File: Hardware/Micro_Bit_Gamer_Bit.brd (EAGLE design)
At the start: 152.4 x 50.8 mm, 35 parts, among them J1 Pokehome, J2 Pokehome, J3 Pokehome, J4 Pokehome, J5 Pokehome, J6 Pokehome, J7 Pokehome, J8 Pokehome, U1 micro:bit

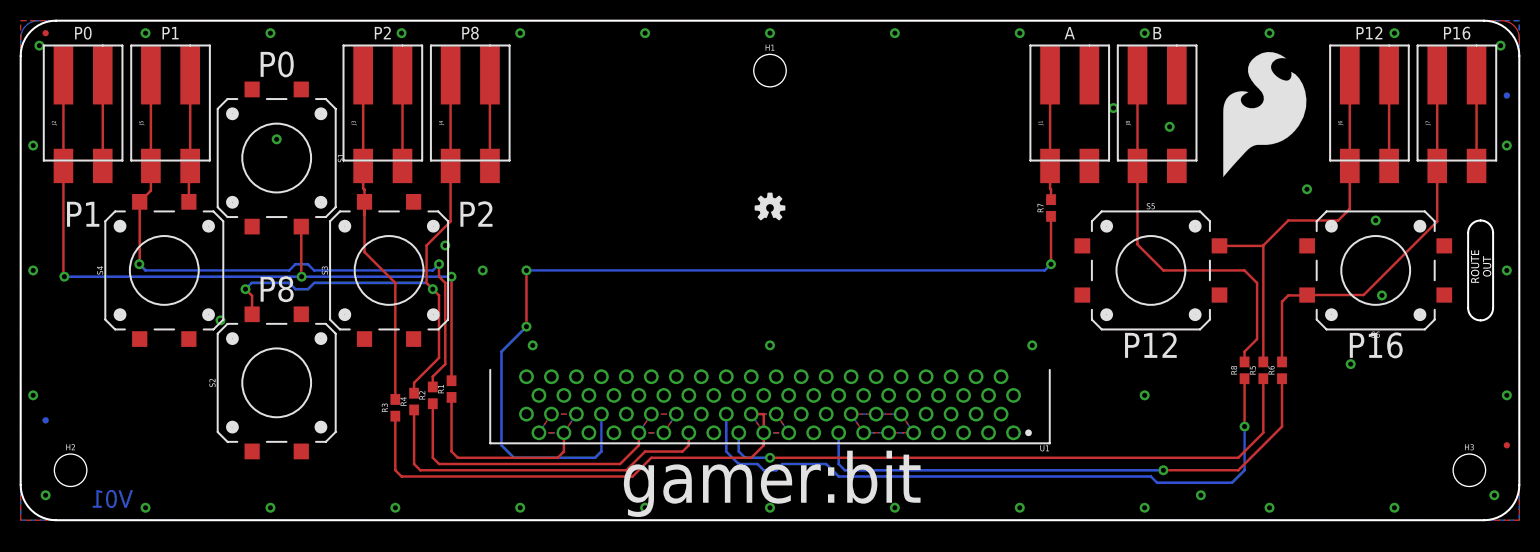
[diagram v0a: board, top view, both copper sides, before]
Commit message: Incorporating Edu Feedback.
Pokehomes on back of board.
Touched up logos & markings.
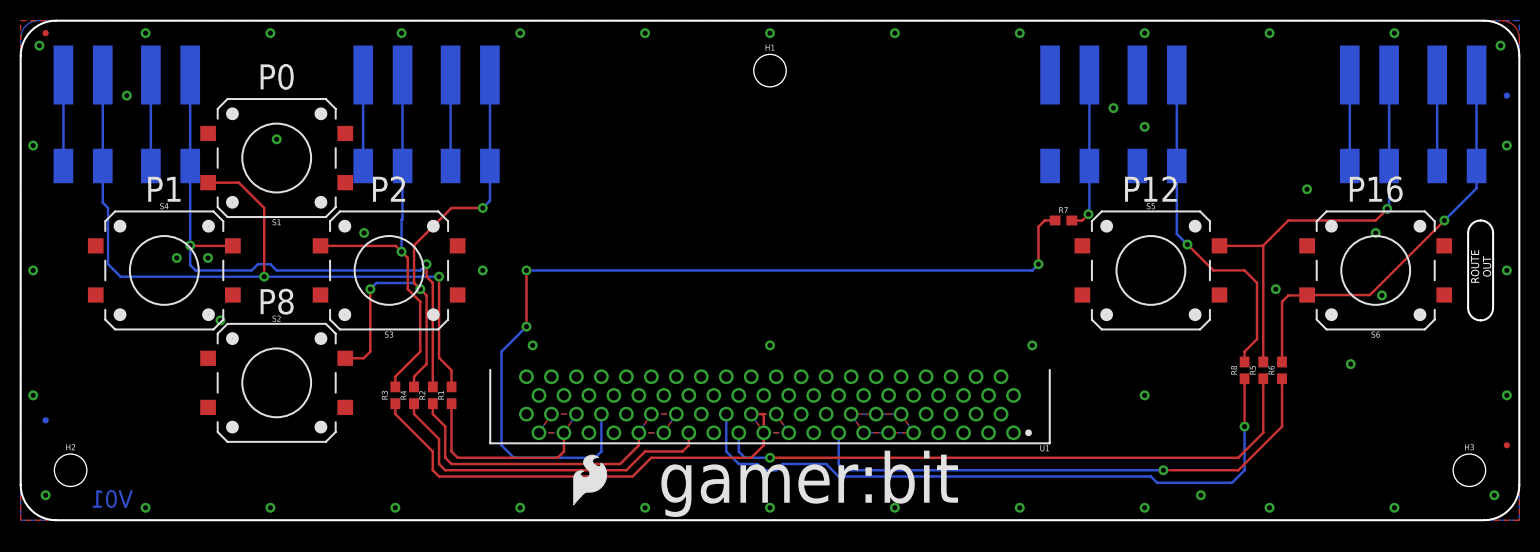
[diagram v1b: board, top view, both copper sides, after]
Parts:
- LOGO1: value SFE_LOGO_FLAME.5_INCH -> SFE_LOGO_FLAME.2_INCH; device SparkFun-Aesthetics:SFE_LOGO_FLAME_.5 -> SparkFun-Aesthetics:SFE_LOGO_FLAME_.2
- moved LOGO1 74.0 mm to (55.9, 1.27)
- moved LOGO3 14.0 mm to (92.7, 34.3)
- moved LOGO2 6.35 mm to (76.2, 25.4), flipped to the bottom
- moved R7 1.80 mm to (106.0, 30.5), turned to 0 degrees
- moved R3 1.27 mm to (38.1, 12.7)
- moved R1 0.64 mm to (43.8, 12.7)
- moved R4 0.63 mm to (40.0, 12.7)
- flipped J1 to the bottom
- flipped J2 to the bottom
- flipped J3 to the bottom
- flipped J4 to the bottom
- flipped J5 to the bottom
- flipped J6 to the bottom
- flipped J7 to the bottom
- flipped J8 to the bottom
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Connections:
- net GND: now also S3.3; no longer S3.1
- net N$4: now also S3.1; no longer S3.3
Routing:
- net N$4: track 35.6 -> 42.2 mm, vias 0 -> 1
- net N$3: track 57.9 -> 52.6 mm, vias 2 -> 3
- net N$6: track 39.6 -> 35.0 mm, vias 0 -> 1
- net N$80: track 40.3 -> 44.2 mm, vias 0 -> 1
- net N$1: track 75.6 -> 79.2 mm, vias 3 -> 2
- net N$7: track 12.7 -> 16.2 mm, vias 0 -> 1
- net N$2: track 64.5 -> 61.5 mm
- net GND: track 58.4 -> 55.5 mm, vias 47 -> 51
- net N$5: track 40.2 -> 42.2 mm, vias 0 -> 1
- net BTN_R: track 49.0 -> 48.0 mm
- net BTN_DN: track 36.0 -> 35.2 mm
- net BTN_L: track 28.8 -> 28.0 mm
- net BTN_UP: track 19.4 -> 18.7 mm
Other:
- board text added: "sparkfun.com/microbit"

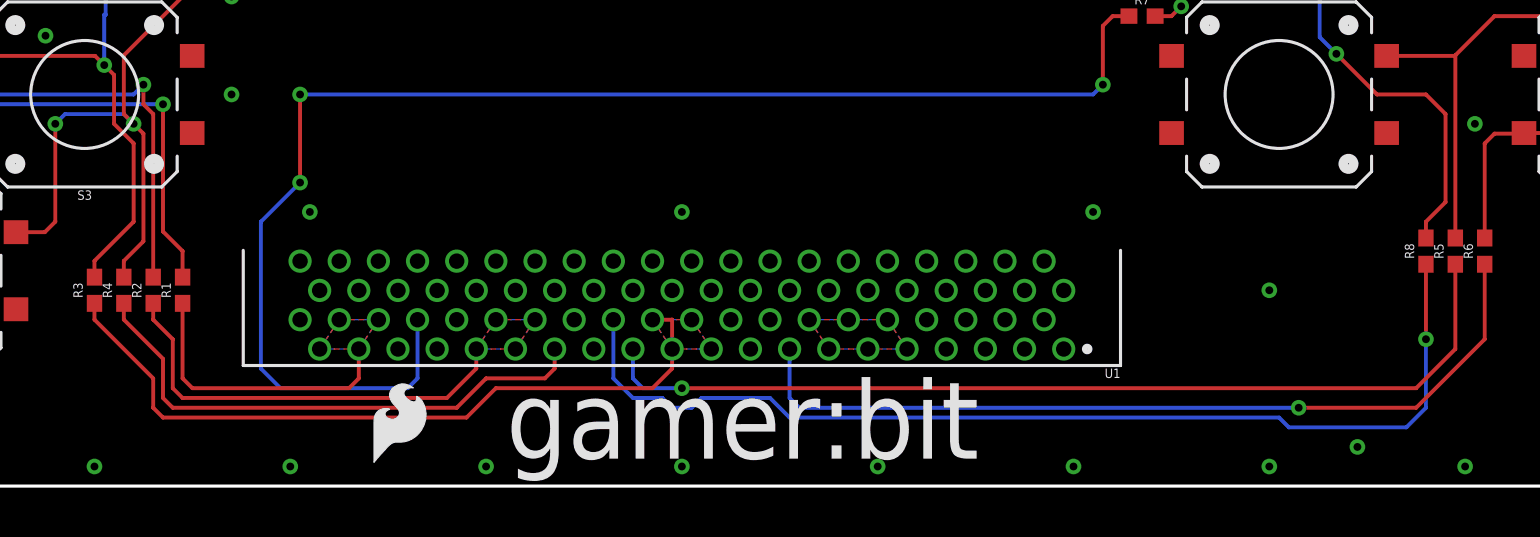
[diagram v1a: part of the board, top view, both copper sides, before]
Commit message: Changed name font to match other microbit boards
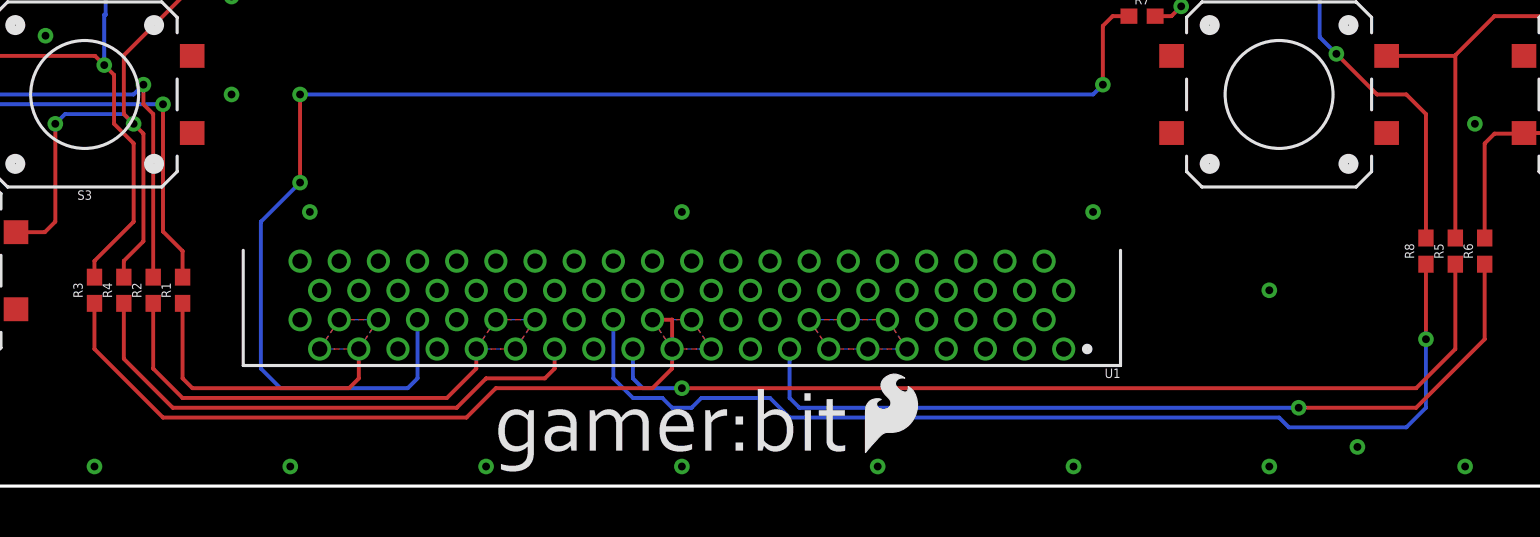
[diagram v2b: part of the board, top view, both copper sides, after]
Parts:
- added U$2, U$3: LOGO-GAMERBIT, Micro_Bit_Parts:LOGO-GAMERBIT
- moved LOGO1 31.9 mm to (87.8, 1.91)
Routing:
- net N$6: track 35.0 -> 33.2 mm
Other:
- board text removed: "gamer:bit"
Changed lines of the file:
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@@
 <setting verticaltext="up"/>
 </settings>
-<grid distance="0.025" unitdist="inch" unit="inch" style="lines" multiple="1" display="yes" altdistance="0.005" altunitdist="inch" altunit="inch"/>
+<grid distance="0.05" unitdist="inch" unit="inch" style="lines" multiple="1" display="yes" altdistance="0.005" altunitdist="inch" altunit="inch"/>
 <layers>
 <layer number="1" name="Top" color="4" fill="1" visible="yes" active="yes"/>
@@
 <layer number="22" name="bPlace" color="14" fill="1" visible="yes" active="yes"/>
 <layer number="23" name="tOrigins" color="15" fill="1" visible="yes" active="yes"/>
-<layer number="24" name="bOrigins" color="15" fill="1" visible="no" active="yes"/>
-<layer number="25" name="tNames" color="7" fill="1" visible="yes" active="yes"/>
+<layer number="24" name="bOrigins" color="15" fill="1" visible="yes" active="yes"/>
+<layer number="25" name="tNames" color="7" fill="1" visible="no" active="yes"/>
 <layer number="26" name="bNames" color="7" fill="1" visible="no" active="yes"/>
 <layer number="27" name="tValues" color="7" fill="1" visible="no" active="yes"/>
@@
 <layer number="49" name="Reference" color="7" fill="1" visible="no" active="yes"/>
 <layer number="50" name="dxf" color="7" fill="1" visible="no" active="no"/>
-<layer number="51" name="tDocu" color="6" fill="1" visible="yes" active="yes"/>
+<layer number="51" name="tDocu" color="6" fill="1" visible="no" active="yes"/>
 <layer number="52" name="bDocu" color="7" fill="1" visible="no" active="yes"/>
 <layer number="53" name="tGND_GNDA" color="7" fill="9" visible="no" active="no"/>
@@
 <text x="114.935" y="32.385" size="2.54" layer="21" font="vector" ratio="15" align="bottom-center">P12</text>
 <text x="137.795" y="32.385" size="2.54" layer="21" font="vector" ratio="15" align="bottom-center">P16</text>
-<text x="80.137" y="1.778" size="5.08" layer="21" font="vector" ratio="15" align="bottom-center">gamer:bit</text>
 <text x="6.35" y="48.895" size="1.27" layer="22" font="vector" ratio="15" rot="MR0" align="bottom-center">P0</text>
 <text x="15.24" y="48.895" size="1.27" layer="22" font="vector" ratio="15" rot="MR0" align="bottom-center">P1</text>
@@
 <text x="137.16" y="48.895" size="1.27" layer="22" font="vector" ratio="15" rot="MR0" align="bottom-center">P12</text>
 <text x="146.05" y="48.895" size="1.27" layer="22" font="vector" ratio="15" rot="MR0" align="bottom-center">P16</text>
-<text x="76.073" y="28.448" size="3.81" layer="22" font="vector" ratio="15" rot="MR0" align="bottom-center">gamer:bit</text>
 <text x="11.43" y="1.27" size="1.778" layer="16" font="vector" ratio="15" rot="MR0">V01</text>
 <dimension x1="0" y1="50.8" x2="152.4" y2="50.8" x3="76.2" y3="88.265" textsize="1.778" textratio="15" layer="47" unit="inch"/>
@@
 <attribute name="PROD_ID" value="CONN-13512" x="146.05" y="41.275" size="1.778" layer="28" font="vector" ratio="15" rot="MR270" display="off"/>
 </element>
-<element name="LOGO1" library="SparkFun-Aesthetics" package="SFE_LOGO_FLAME_.2" value="SFE_LOGO_FLAME.2_INCH" x="55.88" y="1.27"/>
+<element name="LOGO1" library="SparkFun-Aesthetics" package="SFE_LOGO_FLAME_.2" value="SFE_LOGO_FLAME.2_INCH" x="87.757" y="1.905"/>
 <element name="LOGO2" library="SparkFun-Aesthetics" package="OSHW-LOGO-S" value="OSHW-LOGOS" x="76.2" y="25.4" rot="MR0"/>
 <element name="LOGO3" library="SparkFun-Aesthetics" package="SFE_LOGO_NAME_FLAME_.3" value="SFE_LOGO_NAME_FLAME.3_INCH" x="92.71" y="34.29" rot="MR0"/>
@@
 <element name="FD3" library="SparkFun-Aesthetics" package="FIDUCIAL-MICRO" value="FIDUCIALUFIDUCIAL" x="2.54" y="10.16" rot="MR0"/>
 <element name="FD4" library="SparkFun-Aesthetics" package="FIDUCIAL-MICRO" value="FIDUCIALUFIDUCIAL" x="151.13" y="43.18" rot="MR0"/>
+<element name="U$2" library="Micro_Bit_Parts" package="LOGO-GAMERBIT" value="LOGO-GAMERBIT" x="64.135" y="0.762"/>
+<element name="U$3" library="Micro_Bit_Parts" package="LOGO-GAMERBIT" value="LOGO-GAMERBIT" x="87.63" y="27.813" rot="MR0"/>
 </elements>
 <signals>
@@
 <wire x1="60.96" y1="5.715" x2="43.815" y2="5.715" width="0.254" layer="1"/>
 <contactref element="R2" pad="1"/>
-<wire x1="41.91" y1="11.85" x2="41.91" y2="10.795" width="0.254" layer="1"/>
-<wire x1="41.91" y1="10.795" x2="43.18" y2="9.525" width="0.254" layer="1"/>
-<wire x1="43.18" y1="9.525" x2="43.18" y2="6.35" width="0.254" layer="1"/>
-<wire x1="43.18" y1="6.35" x2="43.815" y2="5.715" width="0.254" layer="1"/>
+<wire x1="41.91" y1="11.85" x2="41.91" y2="7.62" width="0.254" layer="1"/>
+<wire x1="41.91" y1="7.62" x2="43.815" y2="5.715" width="0.254" layer="1"/>
 </signal>
 <signal name="BTN_R">
@@
 <wire x1="62.23" y1="4.445" x2="42.545" y2="4.445" width="0.254" layer="1"/>
 <contactref element="R3" pad="1"/>
-<wire x1="42.545" y1="4.445" x2="41.91" y2="5.08" width="0.254" layer="1"/>
-<wire x1="38.1" y1="11.85" x2="38.1" y2="10.795" width="0.254" layer="1"/>
-<wire x1="38.1" y1="10.795" x2="41.91" y2="6.985" width="0.254" layer="1"/>
-<wire x1="41.91" y1="6.985" x2="41.91" y2="5.08" width="0.254" layer="1"/>
+<wire x1="38.1" y1="11.85" x2="38.1" y2="8.89" width="0.254" layer="1"/>
+<wire x1="38.1" y1="8.89" x2="42.545" y2="4.445" width="0.254" layer="1"/>
 </signal>
 <signal name="BTN_DN">
@@
 <wire x1="61.595" y1="5.08" x2="43.18" y2="5.08" width="0.254" layer="1"/>
 <contactref element="R4" pad="1"/>
-<wire x1="40.005" y1="11.85" x2="40.005" y2="10.795" width="0.254" layer="1"/>
-<wire x1="40.005" y1="10.795" x2="42.545" y2="8.255" width="0.254" layer="1"/>
-<wire x1="42.545" y1="8.255" x2="42.545" y2="5.715" width="0.254" layer="1"/>
-<wire x1="42.545" y1="5.715" x2="43.18" y2="5.08" width="0.254" layer="1"/>
+<wire x1="40.005" y1="11.85" x2="40.005" y2="8.255" width="0.254" layer="1"/>
+<wire x1="40.005" y1="8.255" x2="43.18" y2="5.08" width="0.254" layer="1"/>
 </signal>
 <signal name="BTN_P16">
@@
 <contactref element="J8" pad="P4"/>
 <contactref element="J8" pad="P2"/>
-<wire x1="124.46" y1="16.09" x2="124.46" y2="17.145" width="0.254" layer="1"/>
-<wire x1="124.46" y1="17.145" x2="125.73" y2="18.415" width="0.254" layer="1"/>
-<wire x1="125.73" y1="18.415" x2="125.73" y2="24.13" width="0.254" layer="1"/>
-<wire x1="125.73" y1="24.13" x2="124.46" y2="25.4" width="0.254" layer="1"/>
-<wire x1="124.46" y1="25.4" x2="121.285" y2="25.4" width="0.254" layer="1"/>
+<wire x1="124.46" y1="16.09" x2="124.46" y2="24.13" width="0.254" layer="1"/>
+<wire x1="124.46" y1="24.13" x2="123.19" y2="25.4" width="0.254" layer="1"/>
+<wire x1="123.19" y1="25.4" x2="121.285" y2="25.4" width="0.254" layer="1"/>
 <wire x1="118.65" y1="28.035" x2="121.285" y2="25.4" width="0.254" layer="1"/>
 <wire x1="117.57" y1="36.025" x2="117.57" y2="45.275" width="0.254" layer="16"/>

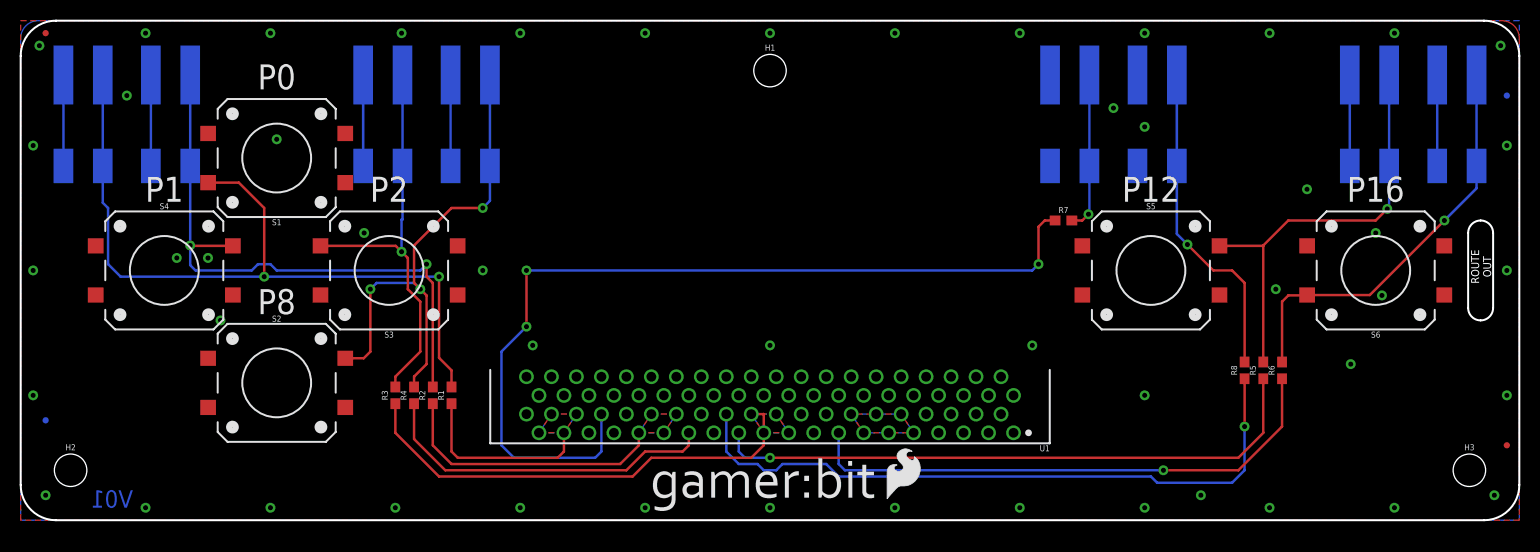
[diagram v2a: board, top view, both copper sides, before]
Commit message: Moved right two buttons together by 0.3 inches
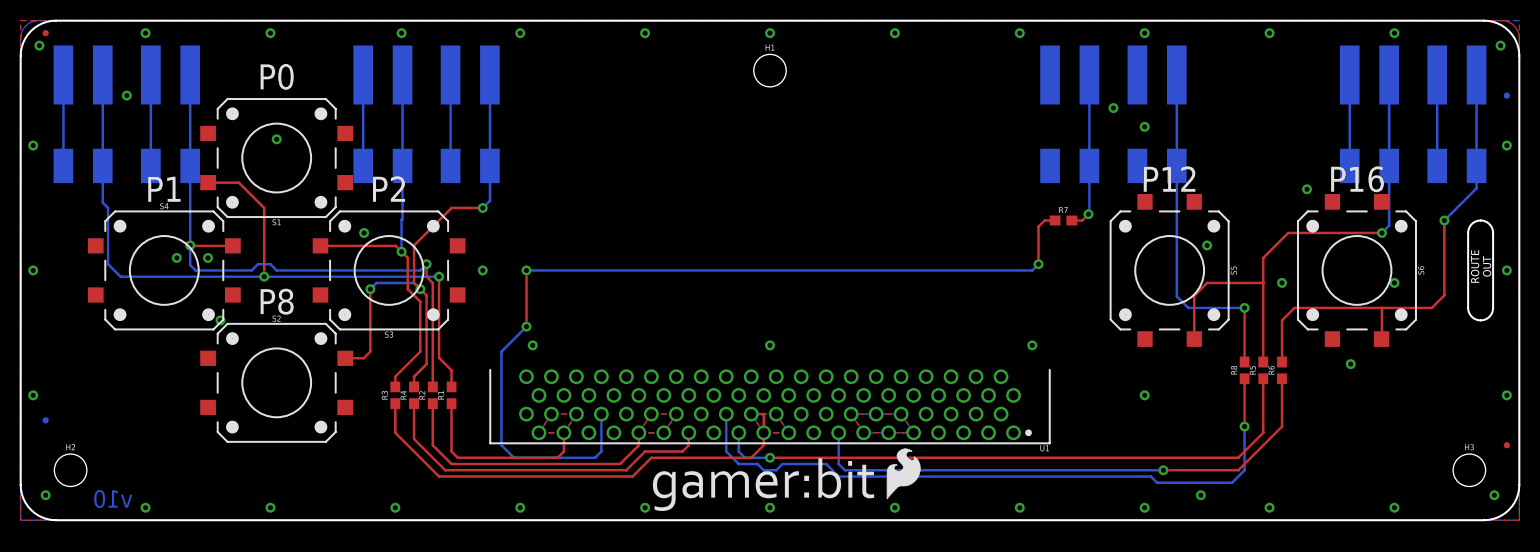
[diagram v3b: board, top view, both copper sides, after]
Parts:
- moved S5 1.91 mm to (116.8, 25.4), turned to 270 degrees
- moved S6 1.91 mm to (135.9, 25.4), turned to 270 degrees
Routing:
- net N$80: track 44.2 -> 52.0 mm
- net N$5: track 42.2 -> 48.7 mm
- net N$6: track 33.2 -> 35.4 mm
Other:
- board text added: "v10"
- board text removed: "V01"

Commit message: Created version 1.0
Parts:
- LOGO2: value OSHW-LOGOS -> OSHW-LOGOL; device SparkFun-Aesthetics:OSHW-LOGO-S -> SparkFun-Aesthetics:OSHW-LOGO-L
- moved FRAME1 16.5 mm to (32.4, -19.7)
- moved U$1 16.5 mm to (21.0, -25.4)
- moved U$3 1.27 mm to (87.6, 29.1)
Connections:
- new net 3.3V: U1.A10, U1.A11, U1.A12, U1.A13, U1.A14, U1.A9
